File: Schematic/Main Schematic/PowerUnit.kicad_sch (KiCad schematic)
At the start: 21 parts, among them Q3 Q_PMOS_DGS, U4 MCP73831-2-OT, U5 TPS61200DRC, U6 LM117_TO3

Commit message: 'Update'
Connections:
- net Vcc 5V: now reaches C2.1, D11.1 (K), Q3.2 (G), R15.1, U4.4 (VDD)
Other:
- note added: "Please place it where you should"
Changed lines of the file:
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@@
+    (stroke (width 0) (type default))
+  )
+  (wire (pts (xy 45.72 89.0524) (xy 49.53 89.0524))
     (stroke (width 0) (type default))
   )
@@
     (stroke (width 0) (type default))
   )
-  (wire (pts (xy 40.64 99.2124) (xy 49.53 99.2124))
+  (wire (pts (xy 36.83 99.06) (xy 45.72 99.06))
     (stroke (width 0) (type default))
   )
@@
     (stroke (width 0) (type default))
   )
-  (wire (pts (xy 49.53 89.0524) (xy 49.53 99.2124))
+  (wire (pts (xy 45.72 89.0524) (xy 45.72 99.06))
     (stroke (width 0) (type default))
   )
@@
     (stroke (width 0) (type default))
   )
+  (text "Please place it where you should\n" (at 20.32 104.14 0)
+    (effects (font (size 1.5 1.5)) (justify left bottom))
+  )
+  (global_label "Vcc 5V" (shape input) (at 36.83 99.06 180) (fields_autoplaced)
+    (effects (font (size 1.27 1.27)) (justify right))
+    (property "Intersheetrefs" "${INTERSHEET_REFS}" (at 27.5983 99.06 0)
+      (effects (font (size 1.27 1.27)) (justify right) hide)
+    )
+  )
   (global_label "3.3V" (shape input) (at 271.78 111.9124 0)

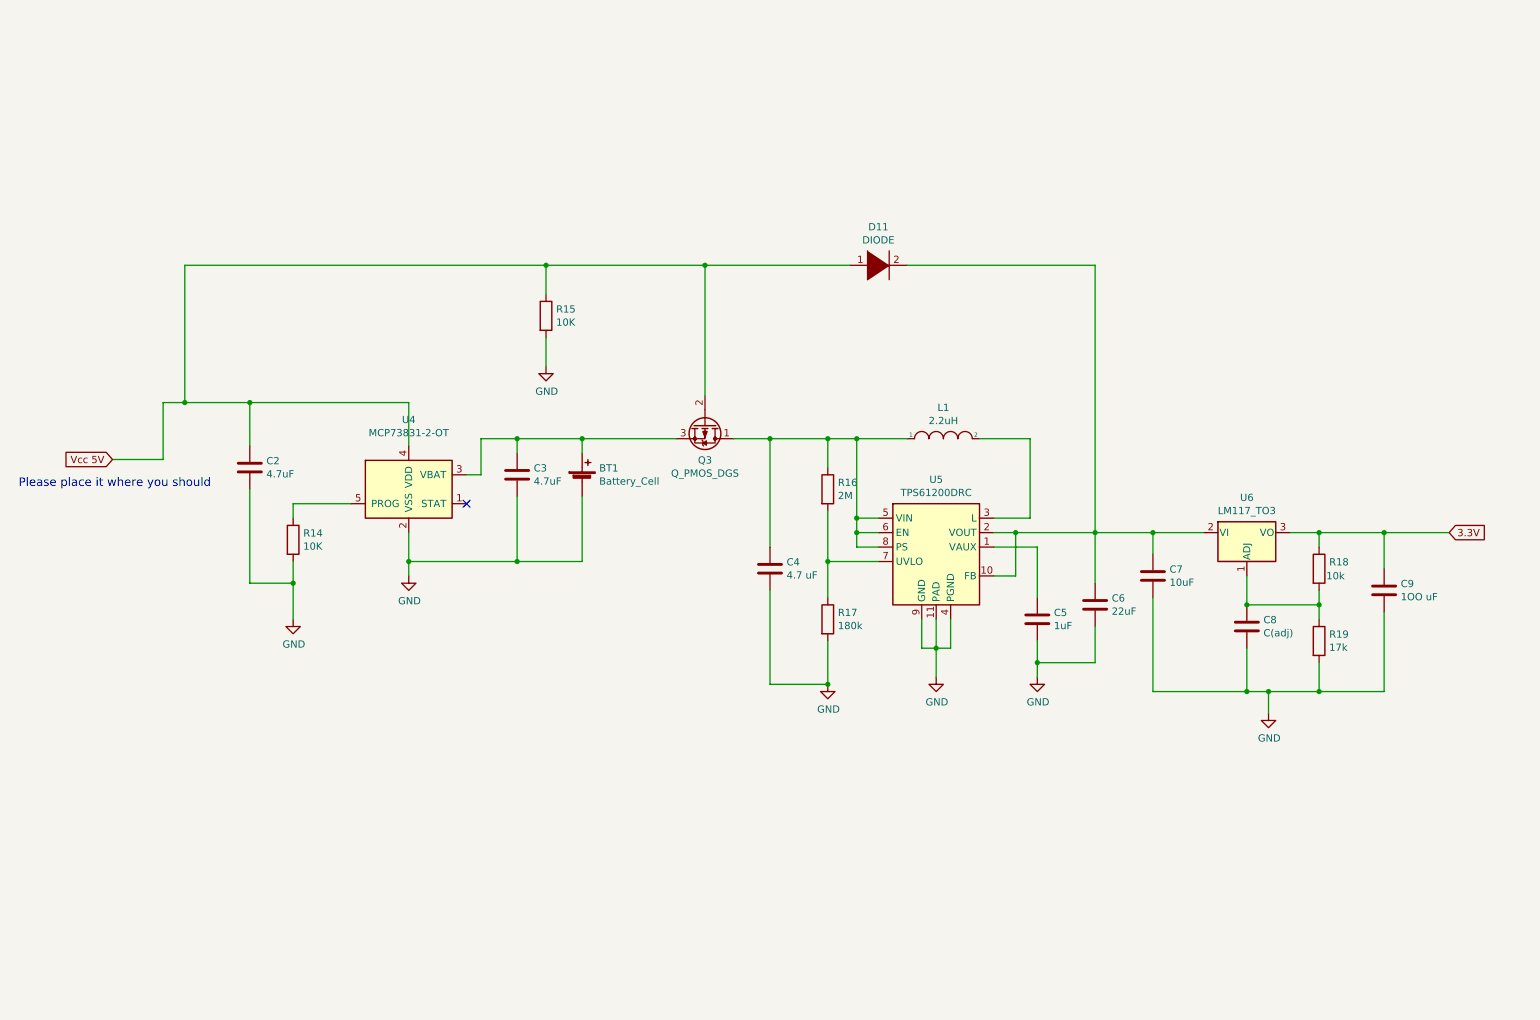
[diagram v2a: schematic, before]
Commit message: I have updated the power management unit
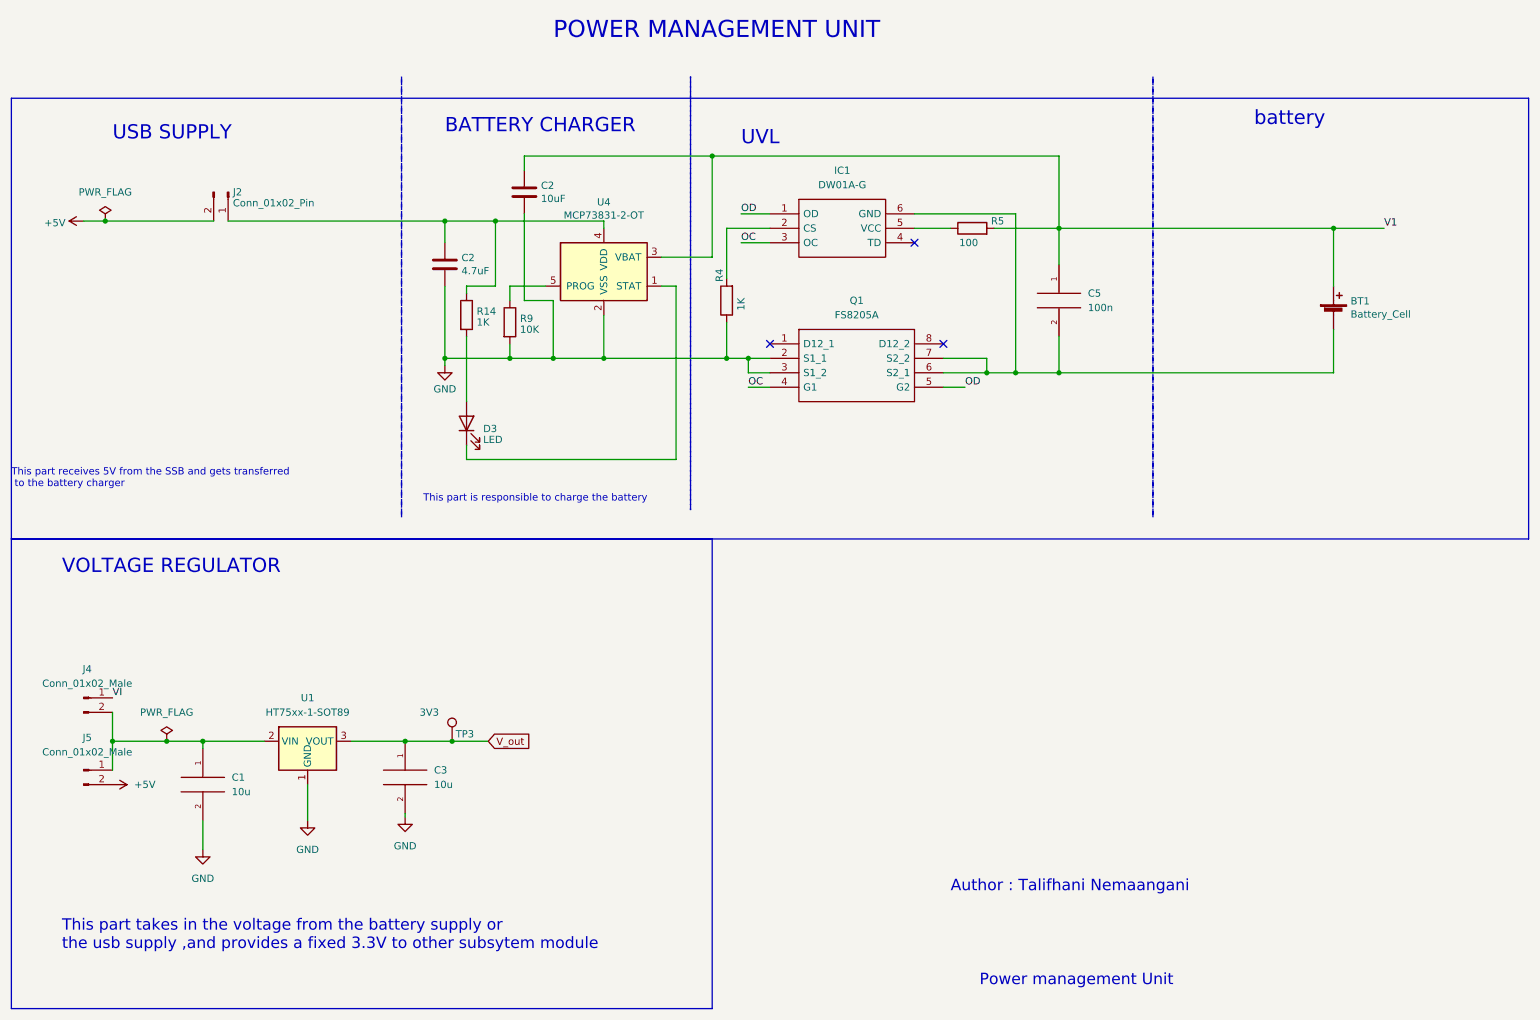
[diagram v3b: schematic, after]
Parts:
- removed C2, C3: 4.7uF, symbol Device:C
- removed C4: 4.7 uF, symbol Device:C
- removed C5: 1uF, symbol Device:C
- removed C6: 22uF, symbol Device:C
- removed C7: 10uF, symbol Device:C
- removed C8: C(adj), symbol Device:C
- removed C9: 1OO uF, symbol Device:C
- removed D11: DIODE, symbol power supplly-rescue:DIODE-pspice
- removed L1: 2.2uH, symbol power supplly-rescue:INDUCTOR-pspice
- removed Q3: Q_PMOS_DGS, symbol Device:Q_PMOS_DGS
- removed R15: 10K, symbol Device:R
- removed R16: 2M, symbol Device:R
- removed R17: 180k, symbol Device:R
- removed R18: 10k, symbol Device:R
- removed R19: 17k, symbol Device:R
- removed U5: TPS61200DRC, Package_SON:Texas_S-PVSON-N10_ThermalVias, symbol Regulator_Switching:TPS61200DRC
- removed U6: LM117_TO3, Package_TO_SOT_THT:TO-3, symbol Regulator_Linear:LM117_TO3
- added C1, C3: 10u, 10uFcapa:CAPC1608X100N, symbol pspice:CAP
- added C2: 10uF, symbol Device:C
- added C2: 4.7uF, symbol Device:C
- added C5: 100n, 10uFcapa:CAPC1608X100N, symbol pspice:CAP
- added D3: LED, symbol Device:LED
- added IC1: DW01A-G, DW:SOT95P280X135-6N, symbol DW01A-G:DW01A-G
- added J2: Conn_01x02_Pin, symbol Connector:Conn_01x02_Pin
- added J4, J5: Conn_01x02_Male, Connector_PinHeader_2.54mm:PinHeader_1x02_P2.54mm_Vertical, symbol Connector:Conn_01x02_Male
- added Q1: FS8205A, FS82:SOP65P640X120-8N, symbol FS8205A:FS8205A
- added R4: 1K, 1K_R:RESC1005X40N, symbol Device:R
- added R5: 100, 100_R:RESC1608X55N, symbol Device:R
- added R9: 10K, symbol Device:R
- added TP3: 3V3, TestPoint:TestPoint_Pad_1.0x1.0mm, symbol Connector:TestPoint
- added U1: HT75xx-1-SOT89, Package_TO_SOT_SMD:SOT-89-3, symbol Regulator_Linear:HT75xx-1-SOT89
- R14: value 10K -> 1K
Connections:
- net Vcc 5V is gone; now on an unnamed net: U4.4 (VDD)
- net GND: now also C1.2, C2.2, C2.2, C3.2, Q1.2 (S1_1), Q1.3 (S1_2), R4.1, R9.2, U1.1 (GND); no longer BT1.2 (-), R14.2
- net at U4.1 (STAT): now also D3.1 (K)
- net V1: now reaches BT1.1 (+), U4.3 (VBAT)
- net V1: now also C2.1, C5.1, R5.2
- net at R14.1: now also C2.1, J2.1 (Pin_1); no longer U4.5 (PROG)
- new net: C1.1, J4.2 (Pin_2), J5.1 (Pin_1), U1.2 (VIN)
- new net: BT1.2 (-), C5.2, IC1.6 (GND), Q1.6 (S2_1), Q1.7 (S2_2)
- new net: D3.2 (A), R14.2
- new net: IC1.5 (VCC), R5.1
- new net: IC1.2 (CS), R4.2
- new net: R9.1, U4.5 (PROG)
- new net +5V: J2.2 (Pin_2), J5.2 (Pin_2)
- new net OC: IC1.3 (OC), Q1.4 (G1)
- new net OD: IC1.1 (OD), Q1.5 (G2)
- new net VI: J4.1 (Pin_1)
- new net V_out: C3.1, TP3.1, U1.3 (VOUT)
- no-connect marks 1 -> 3
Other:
- note added: "Author : Talifhani Nemaangani"
- note added: "BATTERY CHARGER"
- note added: "POWER MANAGEMENT UNIT"
- note added: "Power management Unit"
- note added: "This part is responsible to charge the battery"
- note added: "This part receives 5V from the SSB and gets transferred to the battery charger"
- note added: "This part takes in the voltage from the battery supply or the usb supply ,and provides a fixed 3.3V to other subsytem module"
- note added: "USB SUPPLY"
- note added: "UVL"
- note added: "VOLTAGE REGULATOR"
- note added: "battery"
- note removed: "Please place it where you should"

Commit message: 'update'
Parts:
- removed J2: Conn_01x02_Pin, symbol Connector:Conn_01x02_Pin
- renumbered D3 to D1, R14 to R1, R9 to R2
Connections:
- net +5V: now also C2.1, R1.1, U4.4 (VDD)
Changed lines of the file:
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@@
-    (stroke (width 0) (type default))
-  )
-  (wire (pts (xy 57.15 57.15) (xy 95.25 57.15))
     (stroke (width 0) (type default))
   )
@@
     (stroke (width 0) (type default))
   )
-  (wire (pts (xy 35.56 57.15) (xy 54.61 57.15))
+  (wire (pts (xy 35.56 57.15) (xy 95.25 57.15))
     (stroke (width 0) (type default))
   )
@@
   (symbol (lib_id "power:+5V") (at 31.75 57.15 90) (unit 1)
     (in_bom yes) (on_board yes) (dnp no) (fields_autoplaced)
-    (property "Reference" "#PWR01" (at 35.56 57.15 0)
+    (property "Reference" "#PWR02" (at 35.56 57.15 0)
       (effects (font (size 1.27 1.27)) hide)
     )
@@
   (symbol (lib_id "Device:LED") (at 99.06 92.71 90) (unit 1)
     (in_bom yes) (on_board yes) (dnp no) (fields_autoplaced)
-    (property "Reference" "D3" (at 101.981 93.6538 90)
+    (property "Reference" "D1" (at 101.981 93.6538 90)
       (effects (font (size 1.27 1.27)) (justify right))
     )
@@
   (symbol (lib_id "Device:R") (at 99.06 73.66 0) (unit 1)
     (in_bom yes) (on_board yes) (dnp no) (fields_autoplaced)
-    (property "Reference" "R14" (at 100.838 73.0163 0)
+    (property "Reference" "R1" (at 100.838 73.0163 0)
       (effects (font (size 1.27 1.27)) (justify left))
     )
@@
   (symbol (lib_id "power:GND") (at 95.25 82.55 0) (unit 1)
     (in_bom yes) (on_board yes) (dnp no) (fields_autoplaced)
-    (property "Reference" "#PWR013" (at 95.25 88.9 0)
+    (property "Reference" "#PWR07" (at 95.25 88.9 0)
       (effects (font (size 1.27 1.27)) hide)
     )
@@
     )
   )
-  (symbol (lib_id "Connector:Conn_01x02_Pin") (at 57.15 52.07 270) (unit 1)
-    (in_bom yes) (on_board yes) (dnp no) (fields_autoplaced)
-    (property "Reference" "J2" (at 57.9882 52.0613 90)
-      (effects (font (size 1.27 1.27)) (justify left))
-    )
-    (property "Value" "Conn_01x02_Pin" (at 57.9882 53.9823 90)
-      (effects (font (size 1.27 1.27)) (justify left))
-    )
-    (property "Footprint" "" (at 57.15 52.07 0)
-      (effects (font (size 1.27 1.27)) hide)
-    )
-    (property "Datasheet" "~" (at 57.15 52.07 0)
-      (effects (font (size 1.27 1.27)) hide)
-    )
-    (pin "1")
-    (pin "2")
-    (instances
-      (project "Main Schematic"
-        (path "/81c41bad-bb43-41af-b405-18d135a809b1/297def35-fe1a-4185-9e34-6248c2c818f7"
-          (reference "J7") (unit 1)
-        )
-      )
-    )
-  )
   (symbol (lib_id "Connector:TestPoint") (at 96.52 148.59 0) (unit 1)
     (in_bom yes) (on_board yes) (dnp no)
@@
   (symbol (lib_id "Device:R") (at 106.68 74.93 0) (unit 1)
     (in_bom yes) (on_board yes) (dnp no) (fields_autoplaced)
-    (property "Reference" "R9" (at 108.458 74.2863 0)
-      (effects (font (size 1.27 1.27)) (justify left))
-    )
+    (property "Reference" "R2" (at 108.458 74.2863 0)
+      (effects (font (size 1.27 1.27)) (justify left))
+    )
